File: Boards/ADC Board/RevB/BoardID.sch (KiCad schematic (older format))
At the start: 3 parts

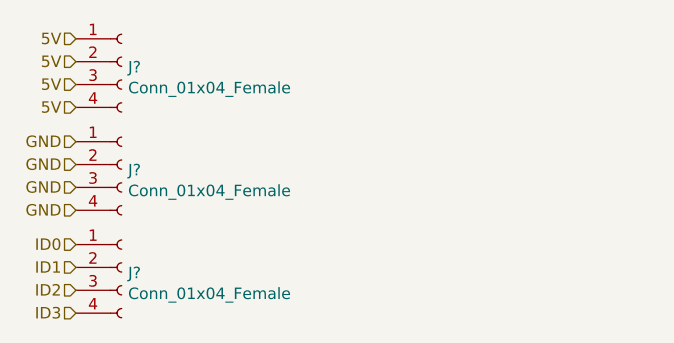
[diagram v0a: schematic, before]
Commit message: Began footprint associations for rev b
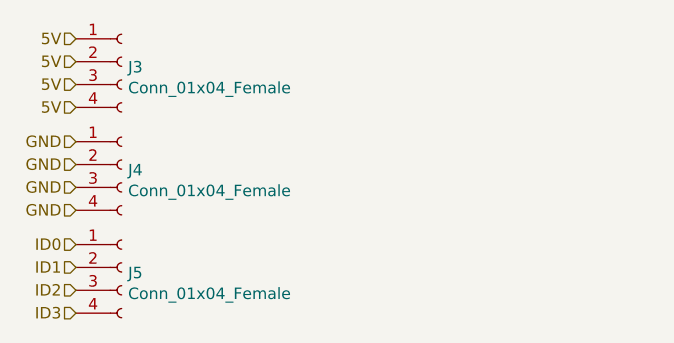
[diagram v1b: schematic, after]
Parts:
- gave numbers to parts that had none: 3
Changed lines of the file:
@@
 $Descr A4 11693 8268
 encoding utf-8
-Sheet 12 13
+Sheet 3 13
 Title ""
 Date ""
@@
 $EndDescr
 $Comp
-L Connector:Conn_01x04_Female J?
+L Connector:Conn_01x04_Female J3
 U 1 1 6231D98E
 P 2850 1400
-F 0 "J?" H 2878 1376 50  0000 L CNN
+F 0 "J3" H 2878 1376 50  0000 L CNN
 F 1 "Conn_01x04_Female" H 2878 1285 50  0000 L CNN
 F 2 "" H 2850 1400 50  0001 C CNN
@@
 $EndComp
 $Comp
-L Connector:Conn_01x04_Female J?
+L Connector:Conn_01x04_Female J4
 U 1 1 6231E88D
 P 2850 1850
-F 0 "J?" H 2878 1826 50  0000 L CNN
+F 0 "J4" H 2878 1826 50  0000 L CNN
 F 1 "Conn_01x04_Female" H 2878 1735 50  0000 L CNN
 F 2 "" H 2850 1850 50  0001 C CNN
@@
 $EndComp
 $Comp
-L Connector:Conn_01x04_Female J?
+L Connector:Conn_01x04_Female J5
 U 1 1 6231EF16
 P 2850 2300
-F 0 "J?" H 2878 2276 50  0000 L CNN
+F 0 "J5" H 2878 2276 50  0000 L CNN
 F 1 "Conn_01x04_Female" H 2878 2185 50  0000 L CNN
 F 2 "" H 2850 2300 50  0001 C CNN

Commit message: Created PCB for Rev B
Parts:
- removed J3, J4, J5: Conn_01x04_Female, symbol Connector:Conn_01x04_Female
- added J22, J3, J4, J5: Conn_01x03_Female, Connector_PinHeader_1.27mm:PinHeader_1x03_P1.27mm_Vertical, symbol Connector:Conn_01x03_Female
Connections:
- net 5V: now also J22.1 (Pin_1), J3.1 (Pin_1), J4.1 (Pin_1), J5.1 (Pin_1)
- net GND: now also J22.3 (Pin_3), J3.3 (Pin_3), J4.3 (Pin_3), J5.3 (Pin_3)
- net ID0: now also J3.2 (Pin_2)
- net ID1: now also J4.2 (Pin_2)
- net ID2: now also J5.2 (Pin_2)
- net ID3: now also J22.2 (Pin_2)
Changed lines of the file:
@@
 Comment4 ""
 $EndDescr
+Text HLabel 4100 1350 0    50   Input ~ 0
+5V
+Text HLabel 4100 1450 0    50   Input ~ 0
+ID0
+Text HLabel 4100 1750 0    50   Input ~ 0
+ID1
+Text HLabel 4100 2050 0    50   Input ~ 0
+ID2
+Text HLabel 4100 2350 0    50   Input ~ 0
+ID3
+Text HLabel 4100 1650 0    50   Input ~ 0
+5V
+Text HLabel 4100 1950 0    50   Input ~ 0
+5V
+Text HLabel 4100 2250 0    50   Input ~ 0
+5V
+Text HLabel 4100 1550 0    50   Input ~ 0
+GND
+Text HLabel 4100 1850 0    50   Input ~ 0
+GND
+Text HLabel 4100 2150 0    50   Input ~ 0
+GND
+Text HLabel 4100 2450 0    50   Input ~ 0
+GND
 $Comp
-L Connector:Conn_01x04_Female J3
-U 1 1 6231D98E
-P 2850 1400
-F 0 "J3" H 2878 1376 50  0000 L CNN
-F 1 "Conn_01x04_Female" H 2878 1285 50  0000 L CNN
-F 2 "" H 2850 1400 50  0001 C CNN
-F 3 "~" H 2850 1400 50  0001 C CNN
-	1    2850 1400
+L Connector:Conn_01x03_Female J3
+U 1 1 62341C12
+P 4300 1450
+F 0 "J3" H 4328 1476 50  0000 L CNN
+F 1 "Conn_01x03_Female" H 4328 1385 50  0000 L CNN
+F 2 "Connector_PinHeader_1.27mm:PinHeader_1x03_P1.27mm_Vertical" H 4300 1450 50  0001 C CNN
+F 3 "~" H 4300 1450 50  0001 C CNN
+	1    4300 1450
 	1    0    0    -1
 $EndComp
 $Comp
-L Connector:Conn_01x04_Female J4
-U 1 1 6231E88D
-P 2850 1850
-F 0 "J4" H 2878 1826 50  0000 L CNN
-F 1 "Conn_01x04_Female" H 2878 1735 50  0000 L CNN
-F 2 "" H 2850 1850 50  0001 C CNN
-F 3 "~" H 2850 1850 50  0001 C CNN
-	1    2850 1850
+L Connector:Conn_01x03_Female J4
+U 1 1 62343054
+P 4300 1750
+F 0 "J4" H 4328 1776 50  0000 L CNN
+F 1 "Conn_01x03_Female" H 4328 1685 50  0000 L CNN
+F 2 "Connector_PinHeader_1.27mm:PinHeader_1x03_P1.27mm_Vertical" H 4300 1750 50  0001 C CNN
+F 3 "~" H 4300 1750 50  0001 C CNN
+	1    4300 1750
 	1    0    0    -1
 $EndComp
 $Comp
-L Connector:Conn_01x04_Female J5
-U 1 1 6231EF16
-P 2850 2300
-F 0 "J5" H 2878 2276 50  0000 L CNN
-F 1 "Conn_01x04_Female" H 2878 2185 50  0000 L CNN
-F 2 "" H 2850 2300 50  0001 C CNN
-F 3 "~" H 2850 2300 50  0001 C CNN
-	1    2850 2300
+L Connector:Conn_01x03_Female J5
+U 1 1 62343834
+P 4300 2050
+F 0 "J5" H 4328 2076 50  0000 L CNN
+F 1 "Conn_01x03_Female" H 4328 1985 50  0000 L CNN
+F 2 "Connector_PinHeader_1.27mm:PinHeader_1x03_P1.27mm_Vertical" H 4300 2050 50  0001 C CNN
+F 3 "~" H 4300 2050 50  0001 C CNN
+	1    4300 2050
 	1    0    0    -1
 $EndComp
-Text HLabel 2650 1300 0    50   Input ~ 0
-5V
-Text HLabel 2650 2200 0    50   Input ~ 0
-ID0
-Text HLabel 2650 2300 0    50   Input ~ 0
-ID1
-Text HLabel 2650 2400 0    50   Input ~ 0
-ID2
-Text HLabel 2650 2500 0    50   Input ~ 0
-ID3
-Text HLabel 2650 1400 0    50   Input ~ 0
-5V
-Text HLabel 2650 1500 0    50   Input ~ 0
-5V
-Text HLabel 2650 1600 0    50   Input ~ 0
-5V
-Text HLabel 2650 1750 0    50   Input ~ 0
-GND
-Text HLabel 2650 1850 0    50   Input ~ 0
-GND
-Text HLabel 2650 1950 0    50   Input ~ 0
-GND
-Text HLabel 2650 2050 0    50   Input ~ 0
-GND
+$Comp
+L Connector:Conn_01x03_Female J22
+U 1 1 62343B2F
+P 4300 2350
+F 0 "J22" H 4328 2376 50  0000 L CNN
+F 1 "Conn_01x03_Female" H 4328 2285 50  0000 L CNN
+F 2 "Connector_PinHeader_1.27mm:PinHeader_1x03_P1.27mm_Vertical" H 4300 2350 50  0001 C CNN
+F 3 "~" H 4300 2350 50  0001 C CNN
+	1    4300 2350
+	1    0    0    -1
+$EndComp
 $EndSCHEMATC
